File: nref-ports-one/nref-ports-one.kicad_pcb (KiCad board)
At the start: 4 copper layers, 88 x 35.5 mm, 150 parts, among them J1 CONN_HEAD, J10 CONN_SPK, J11 POWSW, J2 DM3AT-SF-PEJM5, J3 09452812561, J4 USB_C_Receptacle, J5 Conn_01x10_Pin, J6 Conn_01x14_Pin, J7 Conn_01x12_Pin, J8 PWR, J9 Conn_01x10_Pin, SW1 SW_Push, U1 TPS7A0533PDBZ, U10 LMR51430, U11 TPS66021YBGR, U12 TLV75518PDBV, U13 TMUXHS4212, U14 EQCO5X31C0-I_6NX, U15 LP5907MFX-1.2, U2 TLV320AIC3100, U3 TXS0108EPW, U4 SN74AVC1T45, U5 TPD4E02B04DQA, U6 TPD4E02B04DQA, U7 TPD4E02B04DQA, U8 FUSB302BMPX, U9 PCA9557BS

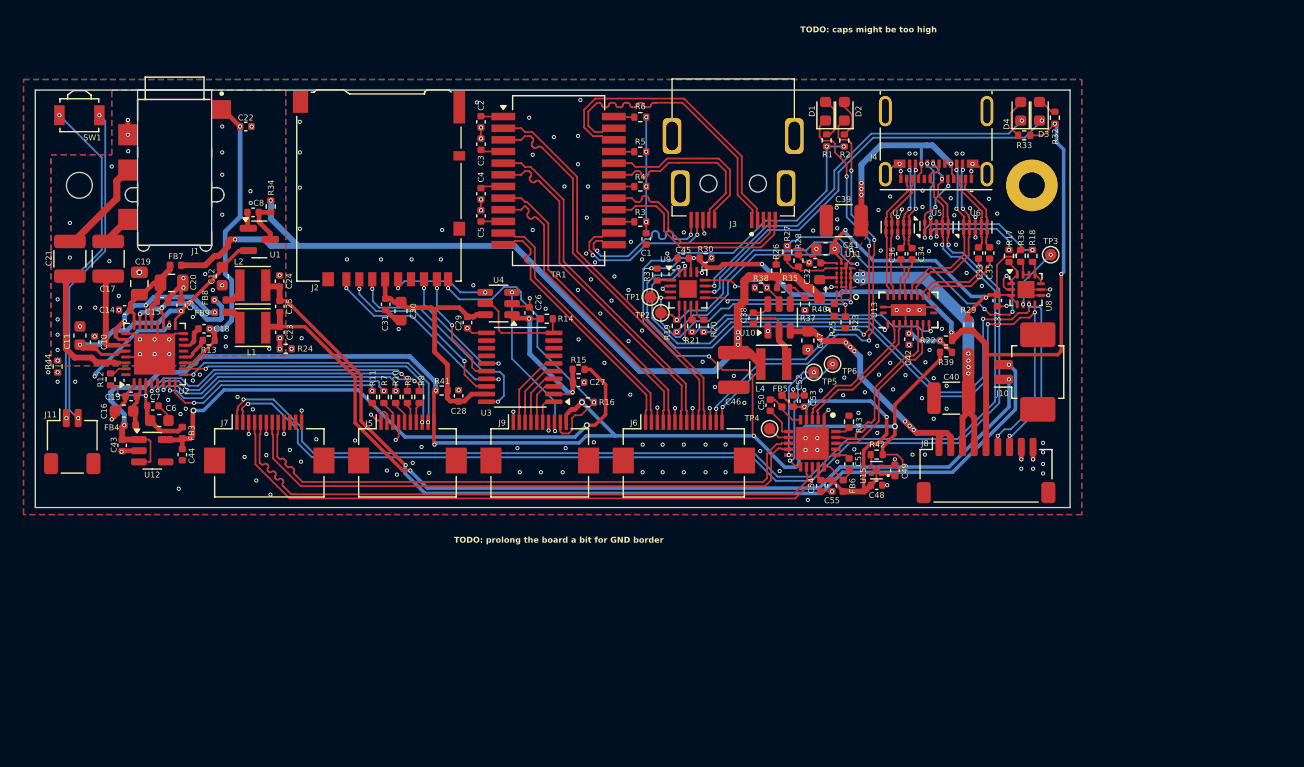
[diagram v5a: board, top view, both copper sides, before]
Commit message: ports-one: exchange pca chip, polish, add sbu header
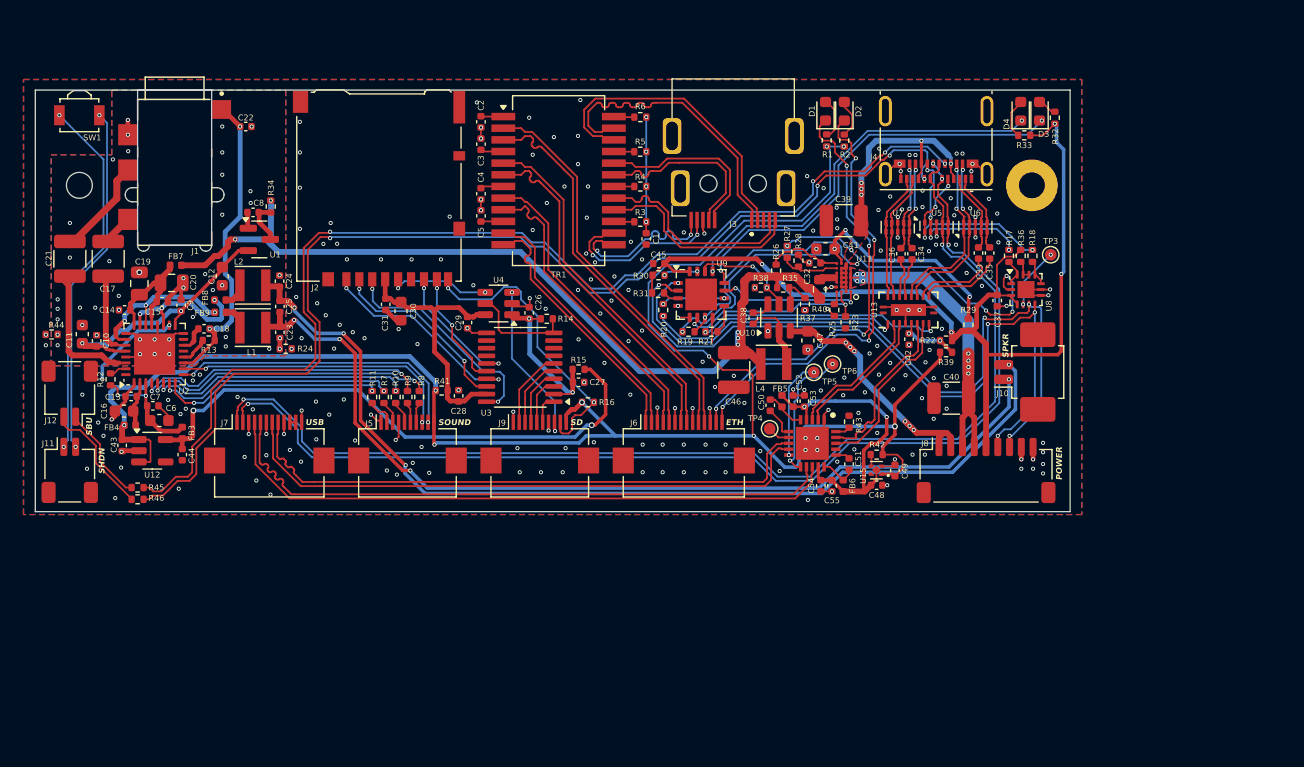
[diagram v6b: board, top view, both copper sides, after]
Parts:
- removed TP1, TP2: TestPoint, TestPoint:TestPoint_Pad_D1.0mm
- added J12: SBU, Connector_JST:JST_SH_SM02B-SRSS-TB_1x02-1MP_P1.00mm_Horizontal, F.Cu at (102.9, 127.7)
- added R45: 33, Resistor_SMD:R_0402_1005Metric, F.Cu at (108.7, 135.7)
- added R46: 33, Resistor_SMD:R_0402_1005Metric, F.Cu at (108.7, 136.7)
- U9: value PCA9557BS -> PCA9557RGVR; footprint Package_DFN_QFN:HVQFN-16-1EP_3x3mm_P0.5mm_EP1.5x1.5mm -> Package_DFN_QFN:Texas_RSA_VQFN-16-1EP_4x4mm_P0.65mm_EP2.7x2.7mm
- moved R30 4.26 mm to (153.0, 117.7)
- moved R20 3.70 mm to (153.4, 120.6)
- moved R44 2.78 mm to (101.4, 122.7), turned to 0 degrees
- moved J11 2.46 mm to (102.9, 134.2)
- moved C45 2.13 mm to (153.0, 116.7)
- moved R21 1.72 mm to (157.5, 122.5), turned to 180 degrees
- moved R31 1.56 mm to (153.0, 119.2), turned to 0 degrees
- moved U9 1.22 mm to (156.6, 119.3)
- moved R19 1.12 mm to (155.6, 122.5), turned to 180 degrees
- moved C11 0.23 mm to (104.0, 122.7)
- moved C10 0.20 mm to (105.2, 123.2)
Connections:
- C37 pad 2: LDO_3V3 -> STANDBY_3V3
- J4 pad A8: unconnected-(J4-SBU1-PadA8) -> SBU_P
- J4 pad B8: unconnected-(J4-SBU2-PadB8) -> SBU_N
- R36 pad 1: LDO_3V3 -> STANDBY_3V3
- U8 pad 3: LDO_3V3 -> STANDBY_3V3
- U8 pad 4: LDO_3V3 -> STANDBY_3V3
- U9 pad 1: Net-(U9-A0) -> RP_SCL0
- U9 pad 10: Net-(D3-K) -> ~{USB_MUX_OE}
- U9 pad 11: Net-(D4-K) -> ~{USB_FAULT}
- U9 pad 12: 5V_AUX_EN -> Net-(D3-K)
- U9 pad 13: Net-(U9-~{RESET}) -> Net-(D4-K)
- U9 pad 14: STANDBY_3V3 -> 5V_AUX_EN
- U9 pad 15: RP_SCL0 -> Net-(U9-~{RESET})
- U9 pad 16: RP_SDA0 -> STANDBY_3V3
- U9 pad 2: GND -> RP_SDA0
- U9 pad 3: GND -> Net-(U9-A0)
- U9 pad 4: USB_SRC_EN -> GND
- U9 pad 5: USB_SINK_EN -> GND
- U9 pad 6: GND -> USB_SRC_EN
- U9 pad 7: USB_MUX_DIR -> USB_SINK_EN
- U9 pad 8: ~{USB_MUX_OE} -> GND
- U9 pad 9: ~{USB_FAULT} -> USB_MUX_DIR
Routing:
- net SBU_P: track 0.00 -> 96.3 mm, vias 0 -> 4
- net SBU_N: track 0.00 -> 95.8 mm, vias 0 -> 4
- net STANDBY_3V3: track 73.4 -> 86.8 mm, vias 6 -> 4
- net Net-(J12-Pin_2): track 0.00 -> 9.96 mm
- net LDO_3V3: track 45.8 -> 36.7 mm
- net Net-(J12-Pin_1): track 0.00 -> 8.28 mm
- net USB_SRC_EN: track 23.5 -> 16.7 mm
- net Net-(U13-~{OE}): track 16.9 -> 21.6 mm
- net ~{USB_MUX_OE}: track 1.53 -> 5.40 mm, vias 0 -> 2
- net RP_SCL0: track 63.6 -> 60.4 mm
- net USB_SINK_EN: track 23.3 -> 20.7 mm
- net Net-(J11-Pin_1): track 28.6 -> 31.2 mm
- net USB_VBUS: track 51.5 -> 54.0 mm
- net Net-(J11-Pin_2): track 27.6 -> 29.9 mm
- net RP_SDA0: track 63.3 -> 61.6 mm
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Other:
- board size 88 x 35.5 mm -> 88 x 35.8 mm
- board text added: "ETH"
- board text added: "POWER"
- board text added: "SBU"
- board text added: "SD"
- board text added: "SHDN"
- board text added: "SOUND"
- board text added: "SPKR"
- board text added: "USB"
- board text removed: "TODO: prolong the board a bit for GND border"

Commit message: ports-one: polishing/part selections
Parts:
- added C56: 0.1uF, Capacitor_SMD:C_0402_1005Metric, F.Cu at (172.0, 128.4)
- added C57: 0.1uF, Capacitor_SMD:C_0402_1005Metric, F.Cu at (171.1, 128.4)
- added C58: 0.1uF, Capacitor_SMD:C_0402_1005Metric, F.Cu at (161.9, 133.9)
- added C59: 0.1uF, Capacitor_SMD:C_0402_1005Metric, F.Cu at (162.9, 133.9)
- U15: footprint Package_SON:Texas_X2SON-4_1x1mm_P0.65mm -> Package_TO_SOT_SMD:SOT-23-5
- moved C49 2.93 mm to (171.9, 136.9), turned to 180 degrees
- moved R42 1.90 mm to (173.4, 132.4), turned to 180 degrees
- moved C48 1.81 mm to (169.7, 135.5), turned to -90 degrees
- moved U15 0.91 mm to (172.3, 134.7)
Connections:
- U14 pad 18: USB1_RE_TXP -> /SDBOP
- U14 pad 19: USB1_RE_TXN -> /SDBON
- U14 pad 8: USB1_RXP -> /SDAOP
- U14 pad 9: USB1_RXN -> /SDAON
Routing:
- net USB1_RE_TXP: track 14.6 -> 8.24 mm
- net USB1_RE_TXN: track 14.6 -> 8.24 mm
- net /SDBOP: track 0.00 -> 5.68 mm
- net /SDBON: track 0.00 -> 5.64 mm
- net USB1_RXP: track 50.5 -> 46.8 mm
- net USB1_RXN: track 50.5 -> 47.5 mm
- net /SDAOP: track 0.00 -> 3.05 mm
- net USB1_DN: track 95.9 -> 98.5 mm
- net /SDAON: track 0.00 -> 2.46 mm
- net +1V2: track 26.3 -> 24.7 mm
- net +3V3: track 154.2 -> 155.5 mm
- net GND: track 75.6 -> 74.7 mm, vias 230 -> 231
